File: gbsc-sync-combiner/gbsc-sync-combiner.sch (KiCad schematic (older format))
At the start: 9 parts, among them J1 DB15_Female_HighDensity_Mount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, J2 JST-XH, J3 JST-XH, U1 74LS86

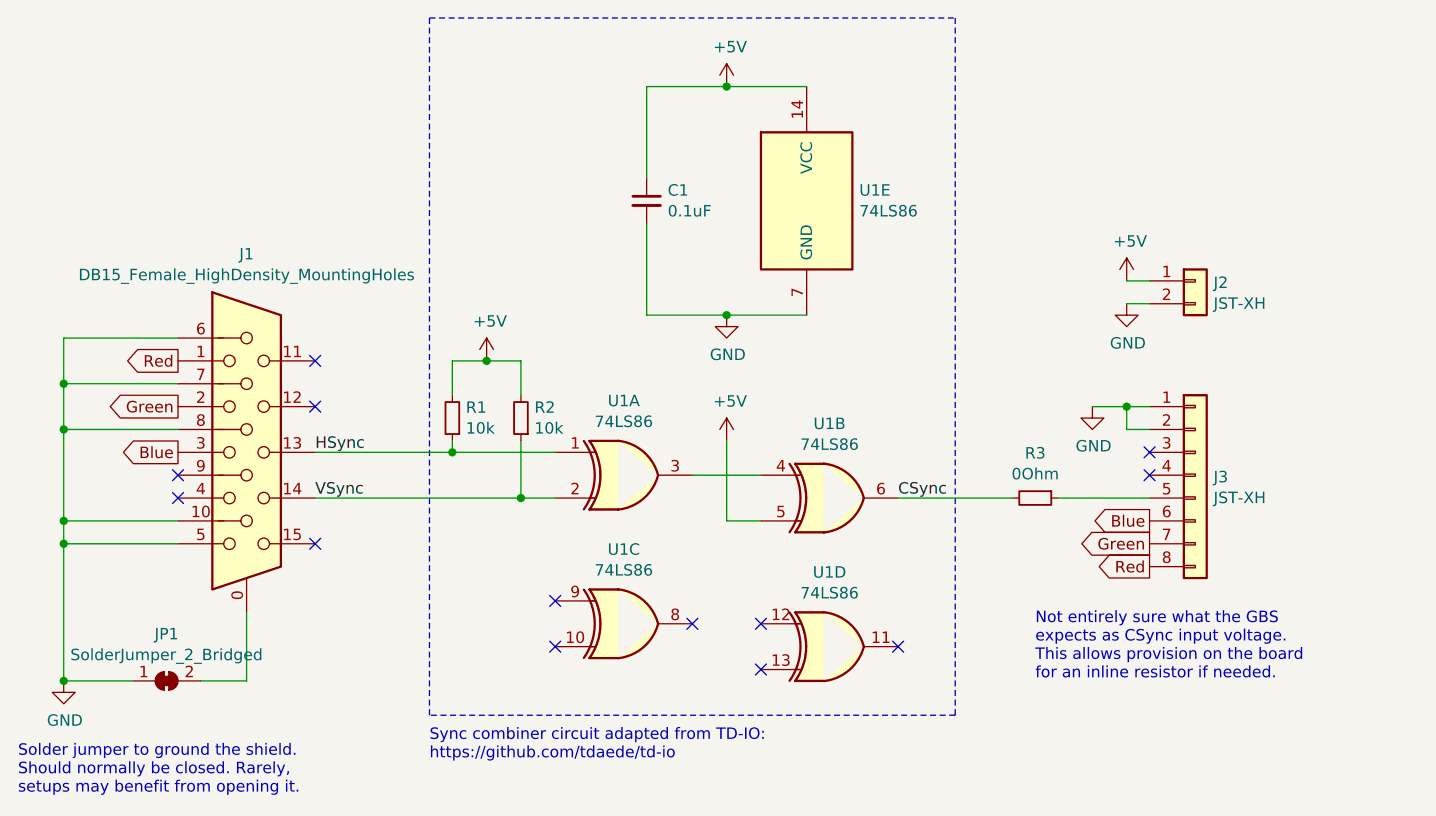
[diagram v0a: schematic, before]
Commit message: Added mounting holes
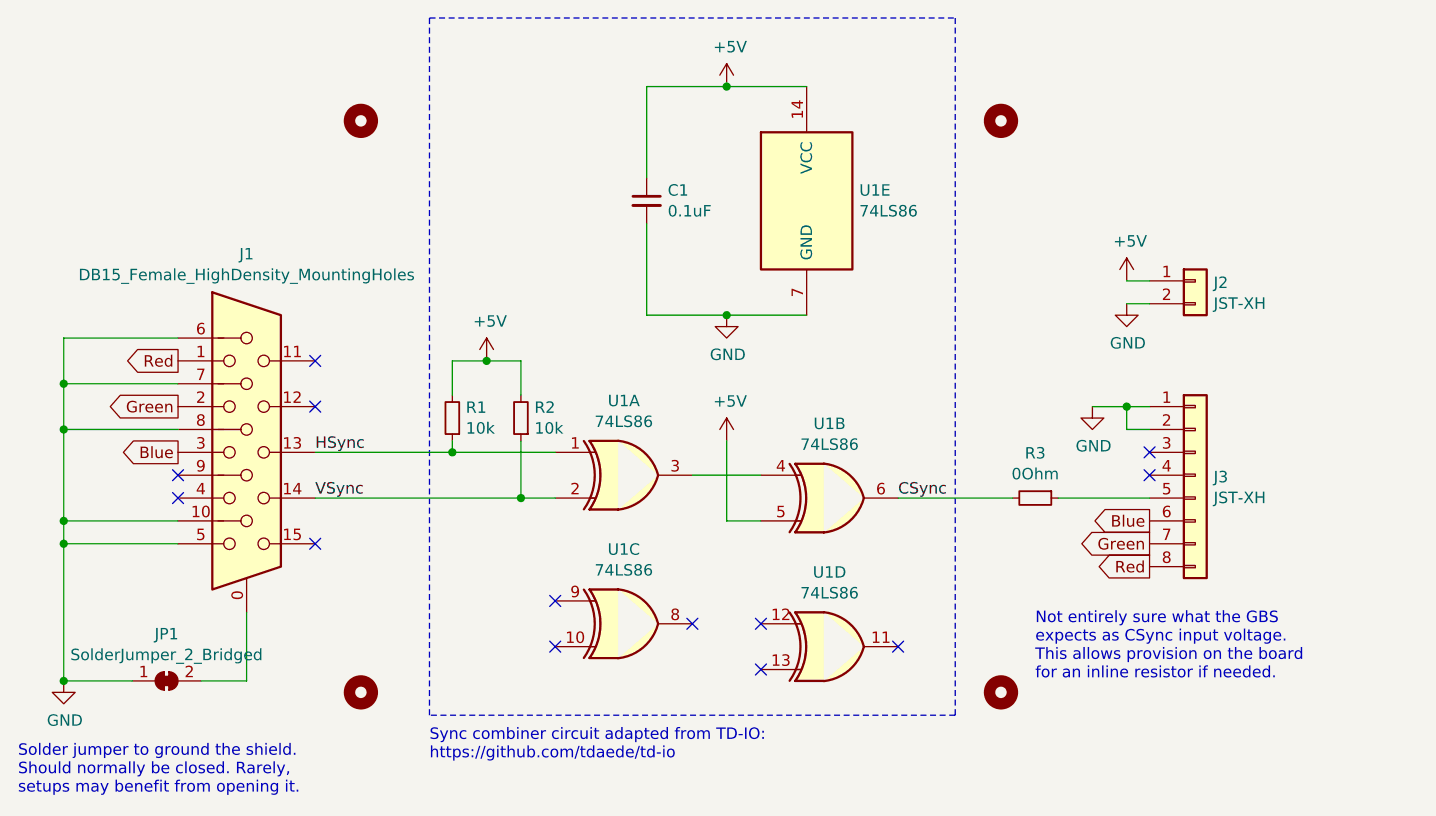
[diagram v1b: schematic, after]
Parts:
- added H1, H2, H3, H4: MountingHole, MountingHole:MountingHole_3.2mm_M3, symbol Mechanical:MountingHole
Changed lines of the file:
@@
 Wire Wire Line
 	5950 2550 5600 2550
-Connection ~ 5950 2550
 Wire Wire Line
 	5600 2550 5600 2950
-Wire Wire Line
-	6300 2550 5950 2550
 $Comp
 L Device:C_Small C1
@@
 Wire Wire Line
 	6700 4350 7200 4350
+Wire Wire Line
+	5950 2550 6300 2550
+Connection ~ 5950 2550
+$Comp
+L Mechanical:MountingHole H2
+U 1 1 618A6908
+P 4350 5200
+F 0 "H2" H 4450 5200 50  0001 L CNN
+F 1 "MountingHole" H 4450 5155 50  0001 L CNN
+F 2 "MountingHole:MountingHole_3.2mm_M3" H 4350 5200 50  0001 C CNN
+F 3 "~" H 4350 5200 50  0001 C CNN
+	1    4350 5200
+	1    0    0    -1
+$EndComp
+$Comp
+L Mechanical:MountingHole H1
+U 1 1 618A8867
+P 4350 2700
+F 0 "H1" H 4450 2700 50  0001 L CNN
+F 1 "MountingHole" H 4450 2655 50  0001 L CNN
+F 2 "MountingHole:MountingHole_3.2mm_M3" H 4350 2700 50  0001 C CNN
+F 3 "~" H 4350 2700 50  0001 C CNN
+	1    4350 2700
+	1    0    0    -1
+$EndComp
+$Comp
+L Mechanical:MountingHole H3
+U 1 1 618A8B98
+P 7150 2700
+F 0 "H3" H 7250 2700 50  0001 L CNN
+F 1 "MountingHole" H 7250 2655 50  0001 L CNN
+F 2 "MountingHole:MountingHole_3.2mm_M3" H 7150 2700 50  0001 C CNN
+F 3 "~" H 7150 2700 50  0001 C CNN
+	1    7150 2700
+	1    0    0    -1
+$EndComp
+$Comp
+L Mechanical:MountingHole H4
+U 1 1 618A904E
+P 7150 5200
+F 0 "H4" H 7250 5200 50  0001 L CNN
+F 1 "MountingHole" H 7250 5155 50  0001 L CNN
+F 2 "MountingHole:MountingHole_3.2mm_M3" H 7150 5200 50  0001 C CNN
+F 3 "~" H 7150 5200 50  0001 C CNN
+	1    7150 5200
+	1    0    0    -1
+$EndComp
 $EndSCHEMATC

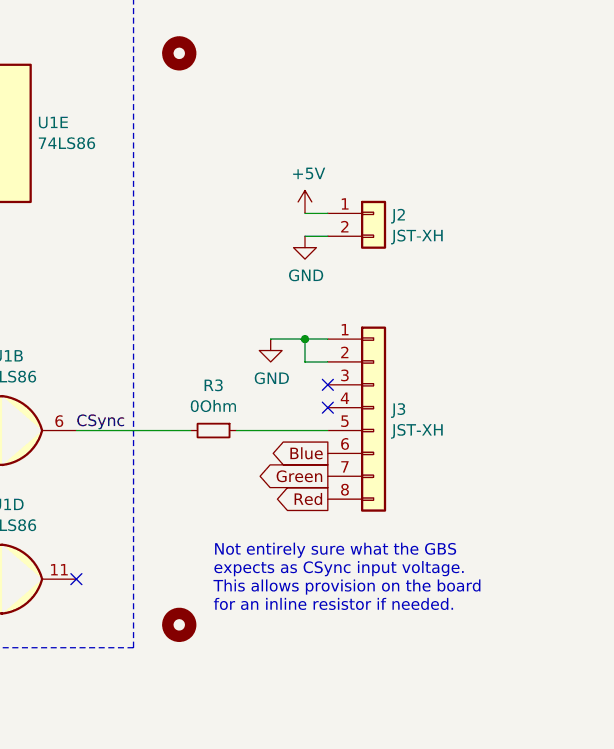
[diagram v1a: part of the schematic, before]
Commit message: Updated connector pinouts to match GBS board
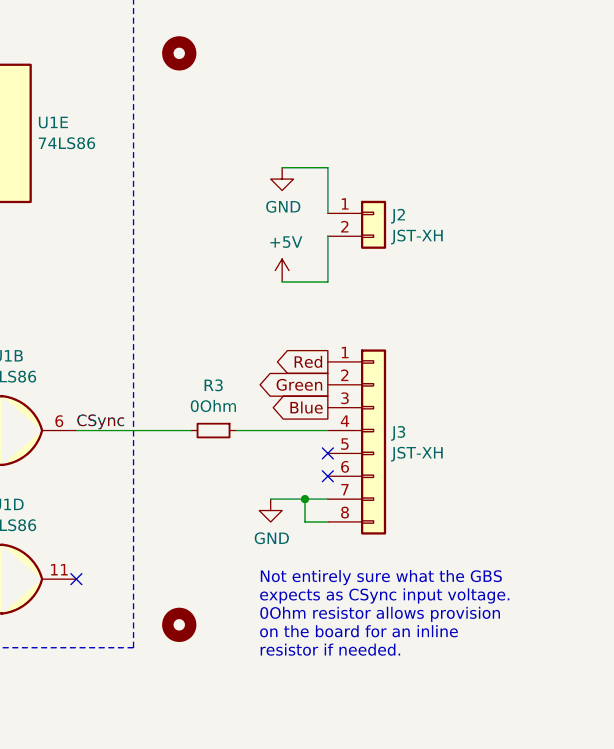
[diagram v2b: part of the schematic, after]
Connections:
- net +5V: now also J2.2 (Pin_2); no longer J2.1 (Pin_1)
- net Blue: now also J3.3 (Pin_3); no longer J3.6 (Pin_6)
- net GND: now also J2.1 (Pin_1), J3.7 (Pin_7), J3.8 (Pin_8); no longer J2.2 (Pin_2), J3.1 (Pin_1), J3.2 (Pin_2)
- net Green: now also J3.2 (Pin_2); no longer J3.7 (Pin_7)
- net Red: now also J3.1 (Pin_1); no longer J3.8 (Pin_8)
- net at J3.4 (Pin_4): now also R3.1
- net at J3.5 (Pin_5): no longer R3.1
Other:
- note added: "Not entirely sure what the GBS \nexpects as CSync input voltage.\n0Ohm resistor allows provision \non the board for an inline \nresistor if needed."
- note removed: "Not entirely sure what the GBS \nexpects as CSync input voltage.\nThis allows provision on the board \nfor an inline resistor if needed."
- moved on the sheet: J3
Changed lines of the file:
@@
 L power:+5V #PWR0106
 U 1 1 617E835C
-P 7700 3400
-F 0 "#PWR0106" H 7700 3250 50  0001 C CNN
-F 1 "+5V" H 7715 3573 50  0000 C CNN
-F 2 "" H 7700 3400 50  0001 C CNN
-F 3 "" H 7700 3400 50  0001 C CNN
-	1    7700 3400
+P 7600 3700
+F 0 "#PWR0106" H 7600 3550 50  0001 C CNN
+F 1 "+5V" H 7615 3873 50  0000 C CNN
+F 2 "" H 7600 3700 50  0001 C CNN
+F 3 "" H 7600 3700 50  0001 C CNN
+	1    7600 3700
 	1    0    0    -1
 $EndComp
@@
 L power:GND #PWR0107
 U 1 1 617E8C2D
-P 7700 3500
-F 0 "#PWR0107" H 7700 3250 50  0001 C CNN
-F 1 "GND" H 7705 3327 50  0000 C CNN
-F 2 "" H 7700 3500 50  0001 C CNN
-F 3 "" H 7700 3500 50  0001 C CNN
-	1    7700 3500
+P 7600 3200
+F 0 "#PWR0107" H 7600 2950 50  0001 C CNN
+F 1 "GND" H 7605 3027 50  0000 C CNN
+F 2 "" H 7600 3200 50  0001 C CNN
+F 3 "" H 7600 3200 50  0001 C CNN
+	1    7600 3200
 	1    0    0    -1
 $EndComp
-Wire Wire Line
-	7800 3400 7700 3400
-Wire Wire Line
-	7800 3500 7700 3500
 $Comp
 L Connector_Generic:Conn_01x08 J3
 U 1 1 617E9E1B
-P 8000 4250
-F 0 "J3" H 8080 4242 50  0000 L CNN
-F 1 "JST-XH" H 8080 4151 50  0000 L CNN
-F 2 "Connector_JST:JST_XH_B8B-XH-A_1x08_P2.50mm_Vertical" H 8000 4250 50  0001 C CNN
-F 3 "~" H 8000 4250 50  0001 C CNN
-	1    8000 4250
+P 8000 4350
+F 0 "J3" H 8080 4342 50  0000 L CNN
+F 1 "JST-XH" H 8080 4251 50  0000 L CNN
+F 2 "Connector_JST:JST_XH_B8B-XH-A_1x08_P2.50mm_Vertical" H 8000 4350 50  0001 C CNN
+F 3 "~" H 8000 4350 50  0001 C CNN
+	1    8000 4350
 	1    0    0    -1
 $EndComp
@@
 L power:GND #PWR0108
 U 1 1 617EAD9D
-P 7550 3950
-F 0 "#PWR0108" H 7550 3700 50  0001 C CNN
-F 1 "GND" H 7555 3777 50  0000 C CNN
-F 2 "" H 7550 3950 50  0001 C CNN
-F 3 "" H 7550 3950 50  0001 C CNN
-	1    7550 3950
+P 7550 4650
+F 0 "#PWR0108" H 7550 4400 50  0001 C CNN
+F 1 "GND" H 7555 4477 50  0000 C CNN
+F 2 "" H 7550 4650 50  0001 C CNN
+F 3 "" H 7550 4650 50  0001 C CNN
+	1    7550 4650
 	1    0    0    -1
 $EndComp
 Wire Wire Line
-	7800 4050 7700 4050
+	7800 4750 7700 4750
 Wire Wire Line
-	7700 4050 7700 3950
+	7700 4750 7700 4650
 Wire Wire Line
-	7700 3950 7800 3950
-NoConn ~ 7800 4150
-NoConn ~ 7800 4250
+	7700 4650 7800 4650
 Wire Wire Line
-	7700 3950 7550 3950
-Connection ~ 7700 3950
+	7700 4650 7550 4650
+Connection ~ 7700 4650
 Text Label 6700 4350 0    50   ~ 0
 CSync
-Text GLabel 7800 4450 0    50   Output ~ 0
+Text GLabel 7800 4250 0    50   Output ~ 0
 Blue
-Text GLabel 7800 4550 0    50   Output ~ 0
+Text GLabel 7800 4150 0    50   Output ~ 0
 Green
-Text GLabel 7800 4650 0    50   Output ~ 0
+Text GLabel 7800 4050 0    50   Output ~ 0
 Red
-Wire Wire Line
-	7400 4350 7800 4350
 $Comp
 L Device:R_Small R3
@@
 	0    1    1    0
 $EndComp
-Text Notes 7300 5150 0    50   ~ 0
-Not entirely sure what the GBS \nexpects as CSync input voltage.\nThis allows provision on the board \nfor an inline resistor if needed.
+Text Notes 7500 5350 0    50   ~ 0
+Not entirely sure what the GBS \nexpects as CSync input voltage.\n0Ohm resistor allows provision \non the board for an inline \nresistor if needed.
 NoConn ~ 3550 4250
 Wire Wire Line
@@
 	1    0    0    -1
 $EndComp
+NoConn ~ 7800 4450
+Wire Wire Line
+	7400 4350 7800 4350
+NoConn ~ 7800 4550
+Wire Wire Line
+	7800 3200 7800 3400
+Wire Wire Line
+	7600 3200 7800 3200
+Wire Wire Line
+	7800 3700 7800 3500
+Wire Wire Line
+	7600 3700 7800 3700
 $EndSCHEMATC
